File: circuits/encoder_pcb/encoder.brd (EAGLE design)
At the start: 22.5 x 16 mm, 15 parts, among them U1 MPU-6050, U2 DS18B20, X1 0.5G-WTX-NPH

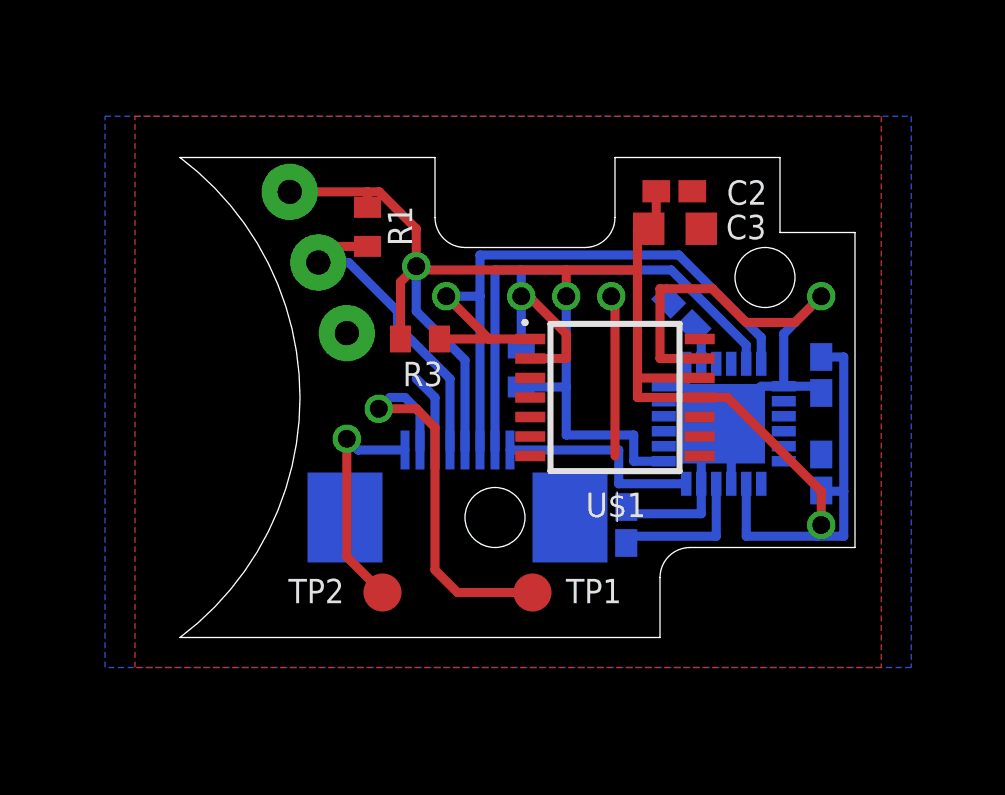
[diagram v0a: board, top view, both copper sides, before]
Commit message: Updated encoder PCB - UNTESTED
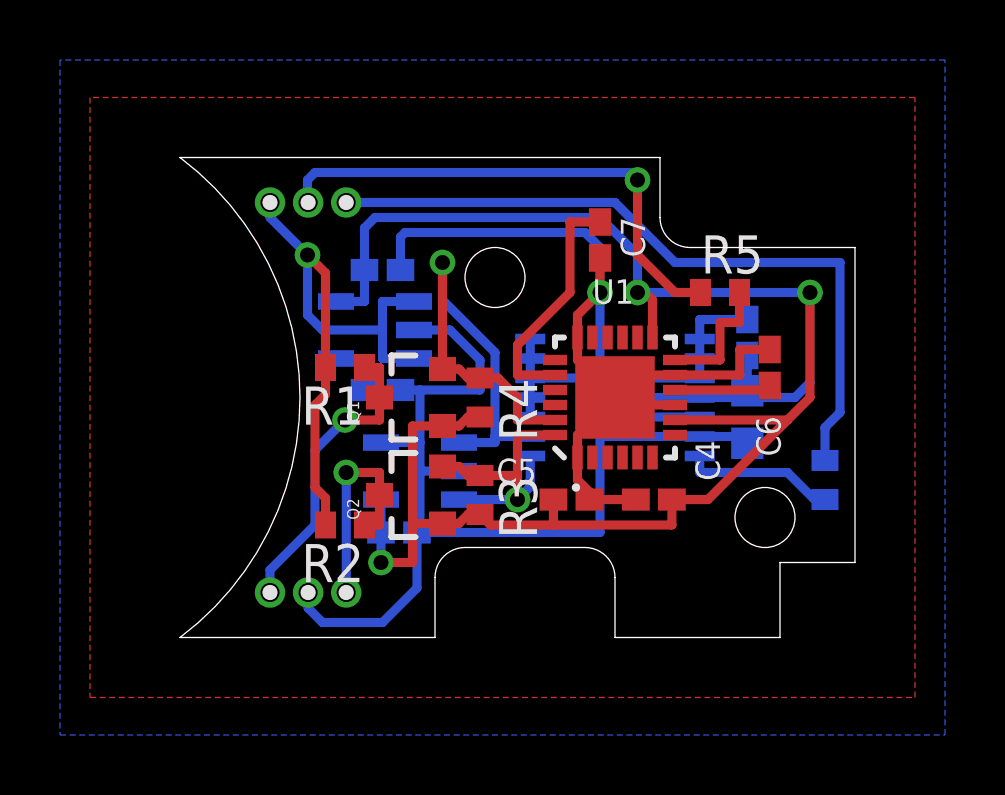
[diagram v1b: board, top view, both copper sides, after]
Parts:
- removed TP1, TP2: TPB1,27, testpad:B1,27
- removed X1: 0.5G-WTX-NPH, FPC_connector_0.5G-WTX-nP:0.5G-WTX-NP
- added C1: 470p, rcl:C0402K
- added C8: 100nF, rcl:C0402K
- added C9: 1u, rcl:C0402K
- added Q1, Q2: 200mA/50V, SparkFun-DiscreteSemi:SOT23-3
- added R4, R5, R6: 10k, rcl:R0402
- added U$2: 24LC16BT-I/OT, 24LC16BT-I_OT:SOT-23-5
- added U$3, U$4: 1X3MALE, headers(.05in):1X3_MALE
- R1, R2, R3: value 4k7 -> 10k
- U2: value DS18B20 -> MIC5219 3.3V; device SparkFun-Sensors:TO-92-AMMO -> SparkFun-PowerIC:SOT23-5
- moved C5 9.31 mm to (13.0, 4.60), flipped to the top, turned to 0 degrees
- moved R2 7.88 mm to (5.50, 3.75), flipped to the top, turned to 180 degrees
- moved C6 7.10 mm to (19.7, 9.00), flipped to the top
- moved C3 6.72 mm to (18.9, 7.35), flipped to the bottom, turned to 270 degrees
- moved C4 5.65 mm to (15.8, 4.60), flipped to the top, turned to 180 degrees
- moved R3 5.57 mm to (10.0, 4.75), turned to 270 degrees
- moved C2 5.45 mm to (18.9, 10.0), flipped to the bottom, turned to 90 degrees
- moved R1 4.75 mm to (5.50, 9.00), turned to 180 degrees
- moved U1 3.73 mm to (14.5, 8.00), flipped to the top, turned to 90 degrees
- moved C7 3.66 mm to (14.0, 13.2), flipped to the top, turned to 270 degrees
- moved U2 2.94 mm to (6.50, 10.2), turned to 270 degrees
- flipped U$1 to the bottom, turned to 180 degrees
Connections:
- removed net 1WIRE: R1.1, U2.2, X1.5
- new net 5V: R1.2, R2.2, U$3.1, U2.1, U2.3
- new net N$5: R6.2, U$1.14
- new net N$6: Q1.3, R1.1, U$4.1
- new net N$7: Q2.3, R2.1, U$4.3
- new net PWM: R6.1, U$3.3
- net 3.3V: now also C8.1, C9.1, Q1.1, Q2.1, R4.2, U$2.4, U2.5; no longer R1.2, R2.2, U2.3, X1.4
- net GND: now also C1.2, C8.2, C9.2, U$2.2, U$2.5, U$4.2, U2.2; no longer U2.1, X1.6
- net INT: now also R5.1, U$3.2; no longer U1.12, X1.1
- net N$1: now also C1.1, U2.4; no longer TP1.TP, X1.7
- net N$3: now also R5.2, U1.12; no longer TP2.TP, X1.8
- net SCL: now also Q1.2, R4.1, U$2.1; no longer R2.1, X1.2
- net SDA: now also Q2.2, U$2.3; no longer X1.3
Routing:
- net GND: track 36.0 -> 82.2 mm, vias 2 -> 1
- net PWM: track 0.00 -> 24.1 mm
- net 5V: track 0.00 -> 20.5 mm, vias 0 -> 1
- net SDA: track 24.1 -> 9.61 mm
- net N$1: track 13.4 -> 2.00 mm, vias 1 -> 0
- net 1WIRE: track 10.5 -> 0.00 mm
- net N$6: track 0.00 -> 10.2 mm, vias 0 -> 1
- net INT: track 7.00 -> 17.1 mm, vias 0 -> 1
- net N$7: track 0.00 -> 7.36 mm, vias 0 -> 1
- net N$2: track 1.34 -> 8.07 mm
- net SCL: track 22.7 -> 17.5 mm
- net N$5: track 0.00 -> 5.10 mm
- net 3.3V: track 65.6 -> 69.1 mm
- net N$3: track 7.71 -> 4.40 mm, vias 1 -> 0
- net N$4: track 4.97 -> 3.31 mm
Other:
- outline, holes or cut-outs redrawn

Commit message: Updated encoder board - UNTESTED
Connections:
- net N$6 renamed SCL_
- net N$7 renamed SDA_
- net 5V: now also U$3.3; no longer U$3.1
- net INT: now also U$3.1; no longer U$3.2
- net PWM: now also U$3.2; no longer U$3.3
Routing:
- net PWM: track 24.1 -> 26.5 mm
- net INT: track 17.1 -> 18.6 mm
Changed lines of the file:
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@@
 <contactref element="U$2" pad="2"/>
 <contactref element="U$2" pad="5"/>
-<contactref element="U$4" pad="2"/>
 <wire x1="11.675" y1="8.65" x2="11.675" y2="9.3" width="0.3048" layer="16"/>
 <wire x1="11.675" y1="9.95" x2="11.675" y2="9.3" width="0.3048" layer="16"/>
@@
 <wire x1="7.9" y1="1.65" x2="6.75" y2="0.5" width="0.3048" layer="16"/>
 <wire x1="6.75" y1="0.5" x2="4.75" y2="0.5" width="0.3048" layer="16"/>
-<wire x1="4.75" y1="0.5" x2="4.27" y2="0.98" width="0.3048" layer="16"/>
-<wire x1="4.27" y1="1.5" x2="4.27" y2="0.98" width="0.3048" layer="16"/>
+<wire x1="4.75" y1="0.5" x2="4.25" y2="1" width="0.3048" layer="16"/>
 <wire x1="8" y1="5.5475" x2="8" y2="6.5" width="0.3048" layer="16"/>
 <wire x1="8" y1="6.5" x2="6.7" y2="6.5" width="0.3048" layer="16"/>
@@
 <wire x1="7.35" y1="12.25" x2="7.35" y2="13.35" width="0.3048" layer="16"/>
 <wire x1="7.9" y1="3.5" x2="7.9" y2="1.65" width="0.3048" layer="16"/>
+<contactref element="U$4" pad="2"/>
+<wire x1="4.25" y1="1" x2="4.27" y2="1" width="0.3048" layer="16"/>
+<wire x1="4.27" y1="1" x2="4.27" y2="1.5" width="0.3048" layer="16"/>
 </signal>
 <signal name="3.3V">
@@
 </signal>
 <signal name="INT">
-<contactref element="U$3" pad="2"/>
-<wire x1="4.27" y1="14.5" x2="4.25" y2="14.52" width="0.3048" layer="16"/>
-<wire x1="4.25" y1="14.52" x2="4.25" y2="15.25" width="0.3048" layer="16"/>
-<wire x1="4.25" y1="15.25" x2="4.5" y2="15.5" width="0.3048" layer="16"/>
-<wire x1="4.5" y1="15.5" x2="15" y2="15.5" width="0.3048" layer="16"/>
-<wire x1="15" y1="15.5" x2="15.25" y2="15.25" width="0.3048" layer="16"/>
-<via x="15.25" y="15.25" extent="1-16" drill="0.5" shape="octagon"/>
-<wire x1="15.25" y1="15.25" x2="15.25" y2="12.75" width="0.3048" layer="1"/>
+<via x="3" y="15.25" extent="1-16" drill="0.5" shape="octagon"/>
 <wire x1="15.25" y1="12.75" x2="16.5" y2="11.5" width="0.3048" layer="1"/>
 <contactref element="R5" pad="1"/>
 <wire x1="17.35" y1="11.5" x2="16.5" y2="11.5" width="0.3048" layer="1"/>
+<contactref element="U$3" pad="1"/>
+<wire x1="15.25" y1="12.75" x2="15.25" y2="14.25" width="0.3048" layer="1"/>
+<wire x1="15.25" y1="14.25" x2="14" y2="15.5" width="0.3048" layer="1"/>
+<wire x1="14" y1="15.5" x2="3" y2="15.5" width="0.3048" layer="1"/>
+<wire x1="3" y1="15.25" x2="3" y2="14.5" width="0.86" layer="16"/>
+<wire x1="3" y1="14.5" x2="3" y2="15.25" width="0.86" layer="1"/>
+<wire x1="3" y1="15.5" x2="3" y2="15.25" width="0.3048" layer="1"/>
 </signal>
 <signal name="N$4">
@@
 </signal>
 <signal name="PWM">
-<contactref element="U$3" pad="3"/>
 <wire x1="22" y1="12.5" x2="16.5" y2="12.5" width="0.3048" layer="16"/>
 <wire x1="16.5" y1="12.5" x2="14.5" y2="14.5" width="0.3048" layer="16"/>
-<wire x1="14.5" y1="14.5" x2="5.54" y2="14.5" width="0.3048" layer="16"/>
 <wire x1="22" y1="12.5" x2="22" y2="7.5" width="0.3048" layer="16"/>
 <contactref element="R6" pad="1"/>
 <wire x1="21.5" y1="5.9" x2="21.5" y2="7" width="0.3048" layer="16"/>
 <wire x1="21.5" y1="7" x2="22" y2="7.5" width="0.3048" layer="16"/>
+<contactref element="U$3" pad="2"/>
+<wire x1="14.5" y1="14.5" x2="7.25" y2="14.5" width="0.3048" layer="16"/>
+<wire x1="7.25" y1="14.5" x2="6.25" y2="15.5" width="0.3048" layer="16"/>
+<wire x1="6.25" y1="15.5" x2="4.75" y2="15.5" width="0.3048" layer="16"/>
+<wire x1="4.27" y1="14.5" x2="4.27" y2="15.02" width="0.3048" layer="16"/>
+<wire x1="4.27" y1="15.02" x2="4.75" y2="15.5" width="0.3048" layer="16"/>
 </signal>
 <signal name="5V">
@@
 <contactref element="R2" pad="2"/>
 <contactref element="R1" pad="2"/>
-<contactref element="U$3" pad="1"/>
 <via x="4.25" y="12.75" extent="1-16" drill="0.5" shape="octagon"/>
 <wire x1="6.75" y1="10.25" x2="6.75" y2="9.3" width="0.3048" layer="16"/>
 <wire x1="7.8001" y1="9.3" x2="6.75" y2="9.3" width="0.3048" layer="16"/>
-<wire x1="4.25" y1="12.75" x2="3" y2="14" width="0.3048" layer="16"/>
-<wire x1="3" y1="14" x2="3" y2="14.5" width="0.3048" layer="16"/>
 <wire x1="4.25" y1="10.75" x2="4.75" y2="10.25" width="0.3048" layer="16"/>
 <wire x1="4.75" y1="10.25" x2="6.75" y2="10.25" width="0.3048" layer="16"/>
@@
 <wire x1="4.85" y1="8.1" x2="4.5" y2="7.75" width="0.3048" layer="1"/>
 <wire x1="4.25" y1="12.75" x2="4.25" y2="10.75" width="0.3048" layer="16"/>
+<contactref element="U$3" pad="3"/>
+<wire x1="4.25" y1="12.75" x2="5.54" y2="14.04" width="0.3048" layer="16"/>
+<wire x1="5.54" y1="14.04" x2="5.54" y2="14.5" width="0.3048" layer="16"/>
 </signal>
 <signal name="N$1">
@@
 <wire x1="6.15" y1="9.3" x2="5.1999" y2="9.3" width="0.3048" layer="16"/>
 </signal>
-<signal name="N$6">
+<signal name="SCL_">
 <contactref element="Q1" pad="3"/>
 <contactref element="R1" pad="1"/>
 <wire x1="6.15" y1="9" x2="6.65" y2="9" width="0.3048" layer="1"/>
 <wire x1="6.65" y1="9" x2="6.65" y2="8" width="0.3048" layer="1"/>
-<contactref element="U$4" pad="1"/>
-<wire x1="3" y1="1.5" x2="3" y2="2.25" width="0.3048" layer="16"/>
-<wire x1="3" y1="2.25" x2="4.5" y2="3.75" width="0.3048" layer="16"/>
-<wire x1="4.5" y1="3.75" x2="4.5" y2="6.25" width="0.3048" layer="16"/>
 <wire x1="4.5" y1="6.25" x2="5.5" y2="7.25" width="0.3048" layer="16"/>
 <via x="5.5" y="7.25" extent="1-16" drill="0.5" shape="octagon"/>
 <wire x1="5.5" y1="7.25" x2="6.65" y2="7.25" width="0.3048" layer="1"/>
 <wire x1="6.65" y1="7.25" x2="6.65" y2="8" width="0.3048" layer="1"/>
-</signal>
-<signal name="N$7">
+<contactref element="U$4" pad="1"/>
+<wire x1="4.5" y1="3.75" x2="3" y2="2.25" width="0.3048" layer="16"/>
+<wire x1="3" y1="2.25" x2="3" y2="1.5" width="0.3048" layer="16"/>
+<wire x1="4.5" y1="6.25" x2="4.5" y2="3.75" width="0.3048" layer="16"/>
+</signal>
+<signal name="SDA_">
 <contactref element="Q2" pad="3"/>
 <contactref element="R2" pad="1"/>

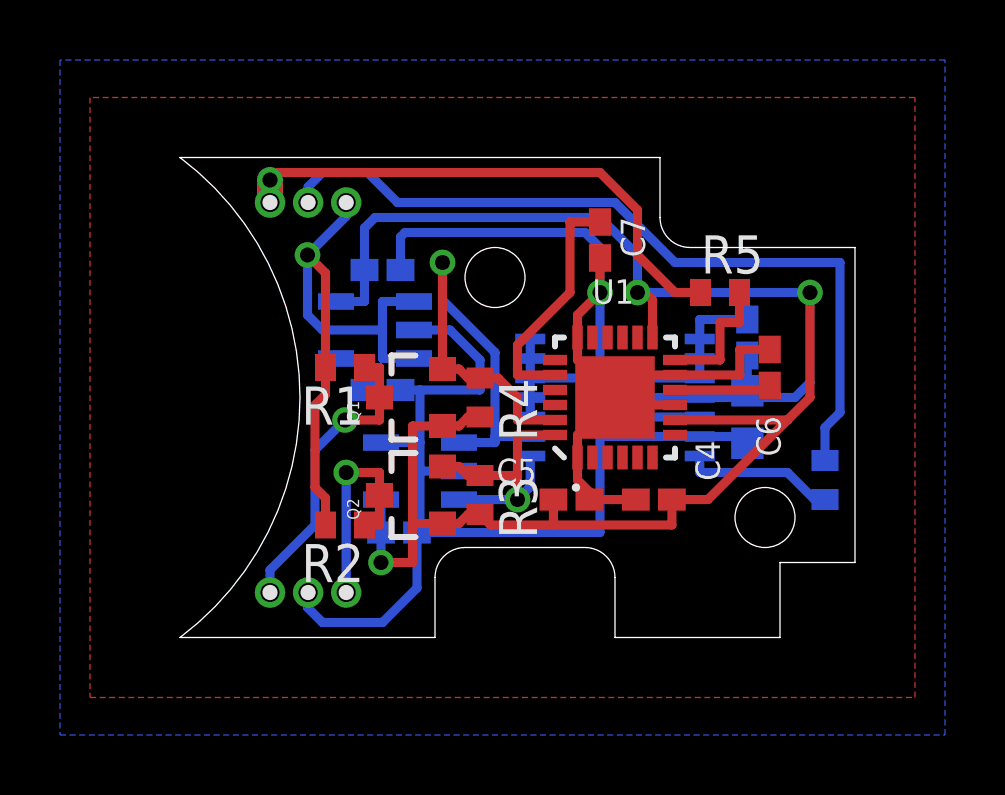
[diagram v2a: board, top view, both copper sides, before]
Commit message: Updated encoder to revision 1 - UNTESTED
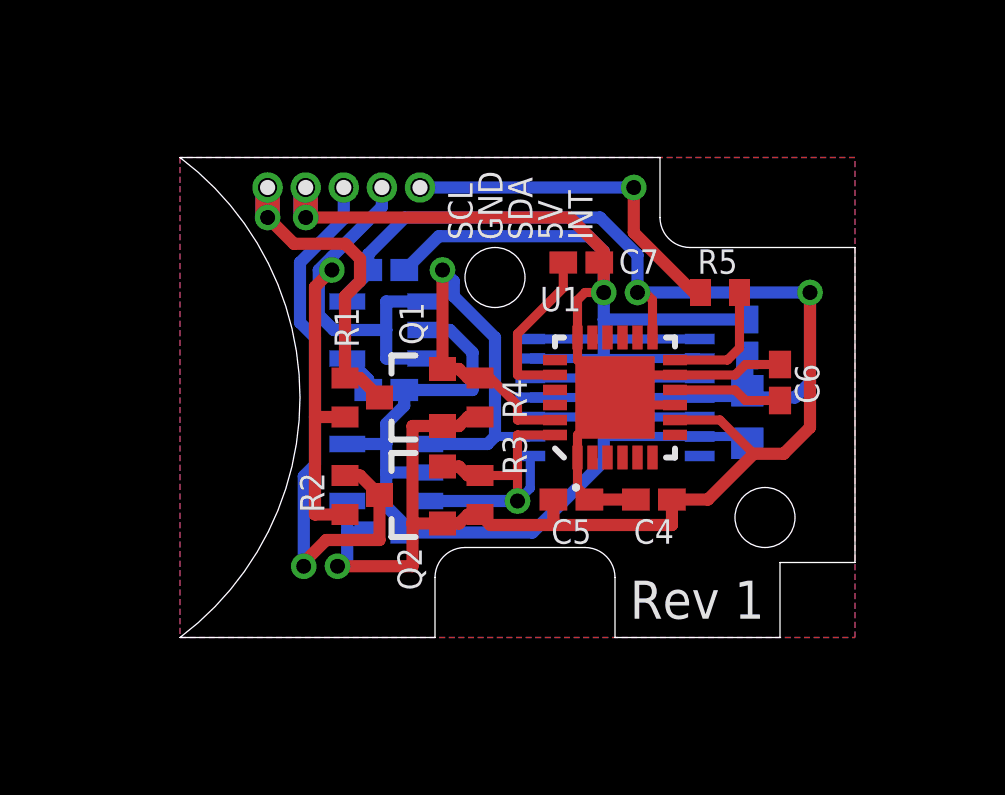
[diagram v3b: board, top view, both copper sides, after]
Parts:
- removed R6: 10k, rcl:R0402
- removed U$2: 24LC16BT-I/OT, 24LC16BT-I_OT:SOT-23-5
- removed U$3, U$4: 1X3MALE, headers(.05in):1X3_MALE
- added U$5: 1X5, headers(.05in):1X5
- added U3: 24LC16BT-I/OT, 24LC16BT-I_OT:SOT-23-5
- moved R1 1.00 mm to (5.50, 8.00), turned to 270 degrees
- moved R2 1.00 mm to (5.50, 4.75), turned to 270 degrees
- moved C7 0.98 mm to (13.4, 12.5), turned to 0 degrees
- moved C6 0.60 mm to (20.0, 8.50)
- moved C8 0.42 mm to (6.88, 3.50)
- moved U2 0.38 mm to (6.88, 10.2)
- moved C1 0.12 mm to (6.88, 8.25)
- moved C9 0.12 mm to (6.88, 12.2)
- renumbered U$1 to U4
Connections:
- removed net N$5: R6.2, U4.14
- removed net PWM: R6.1, U$3.2
- net 3.3V: now also U3.4; no longer U$2.4
- net 5V: now also U$5.2; no longer U$3.3
- net GND: now also U$5.4, U3.2, U3.5; no longer U$2.2, U$2.5, U$4.2
- net INT: now also U$5.1; no longer U$3.1
- net SCL: now also U3.1; no longer U$2.1
- net SCL_: now also U$5.5; no longer U$4.1
- net SDA: now also U3.3; no longer U$2.3
- net SDA_: now also U$5.3; no longer U$4.3
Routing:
- net PWM: track 26.5 -> 0.00 mm
- net GND: track 82.2 -> 100.8 mm, vias 1 -> 2
- net SDA_: track 7.36 -> 19.5 mm
- net INT: track 18.6 -> 11.7 mm
- net N$5: track 5.10 -> 0.00 mm
- net N$2: track 8.07 -> 5.63 mm
- net 5V: track 20.5 -> 22.9 mm
- net 3.3V: track 69.1 -> 71.2 mm
- net SDA: track 9.61 -> 10.8 mm
- net SCL_: track 10.2 -> 11.3 mm
- net N$1: track 2.00 -> 1.34 mm
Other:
- board text added: "5V"
- board text added: "GND"
- board text added: "INT"
- board text added: "Rev 1"
- board text added: "SCL"
- board text added: "SDA"

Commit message: Updated encoder PCB - Tested and working
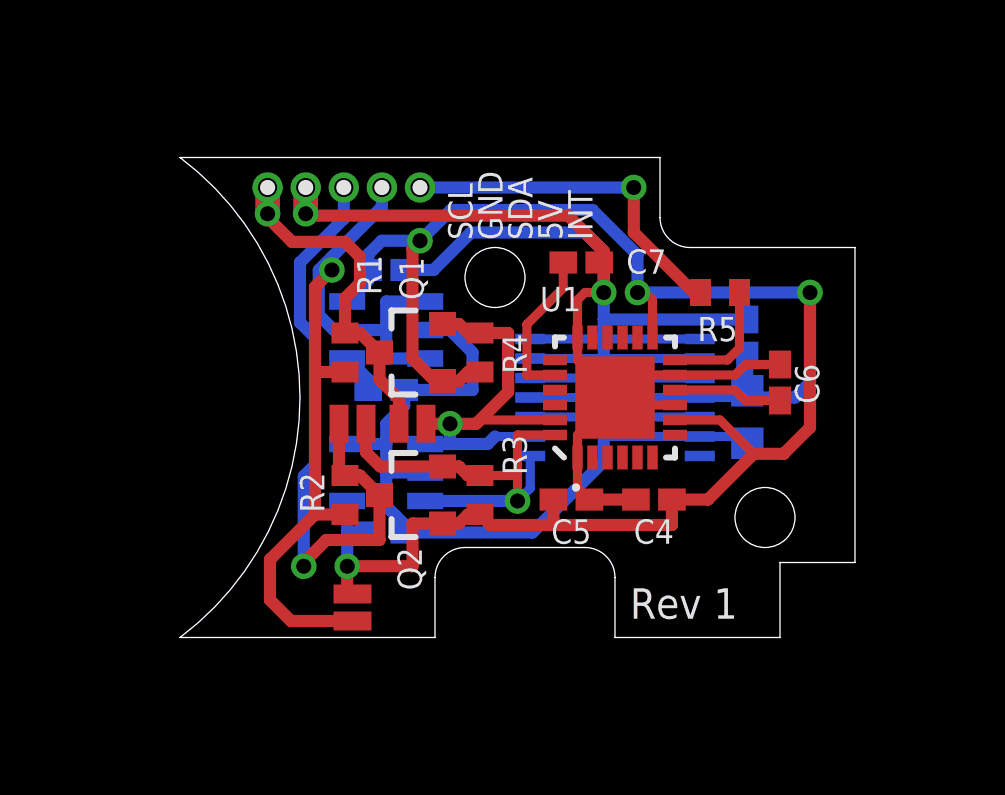
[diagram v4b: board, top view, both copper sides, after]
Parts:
- added JP1, JP2, JP3: JUMPER-PAD-2-NO, SparkFun-Passives:PAD-JUMPER-2-NO_NO_SILK
- moved Q1 1.50 mm to (7.75, 9.50)
- moved R1 1.50 mm to (5.50, 9.50)
- moved R4 1.50 mm to (10.0, 9.50)
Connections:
- net 3.3V: now also JP3.2
- net 5V: now also JP3.1
- net SCL: now also JP1.1
- net SCL_: now also JP1.2
- net SDA: now also JP2.1
- net SDA_: now also JP2.2
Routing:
- net 5V: track 22.9 -> 29.4 mm
- net SDA: track 10.8 -> 14.5 mm
- net SCL: track 17.9 -> 14.4 mm
- net SDA_: track 19.5 -> 21.4 mm
- net 3.3V: track 71.2 -> 72.8 mm, vias 3 -> 4
- net SCL_: track 11.3 -> 12.3 mm
- removed copper zone on layer 1, net GND
- removed copper zone on layer 16, net GND
